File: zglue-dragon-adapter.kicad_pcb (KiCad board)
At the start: 6 copper layers, 25 x 20 mm, 56 parts, among them J1 543630489, J2 543630489, U1 zGlue-Dragon

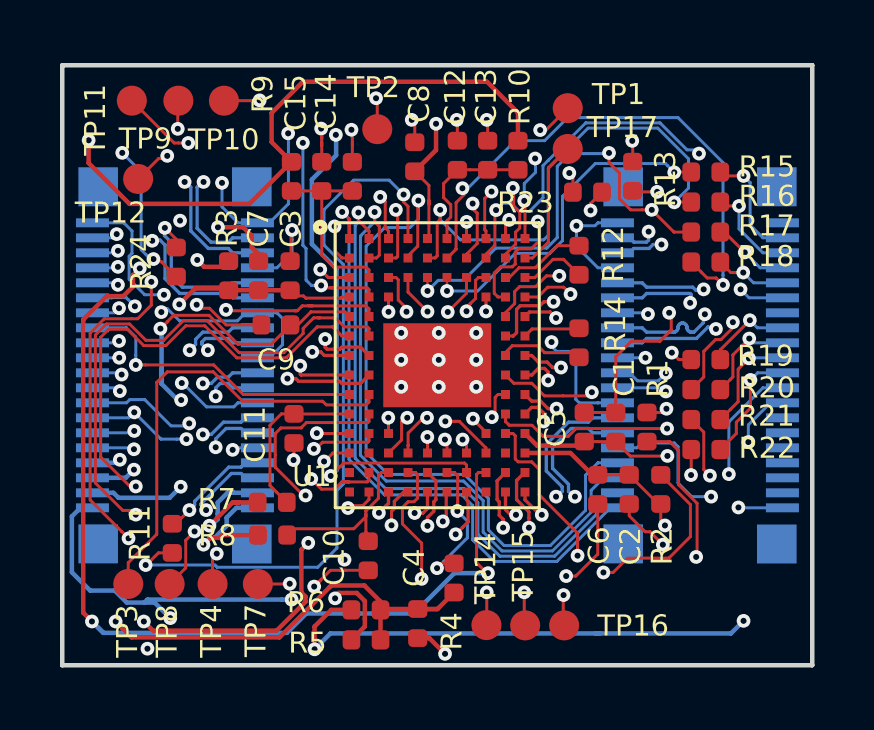
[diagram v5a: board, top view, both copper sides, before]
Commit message: Layout polishing, connected PROC_RST and CTRL_RST to chip via 0R
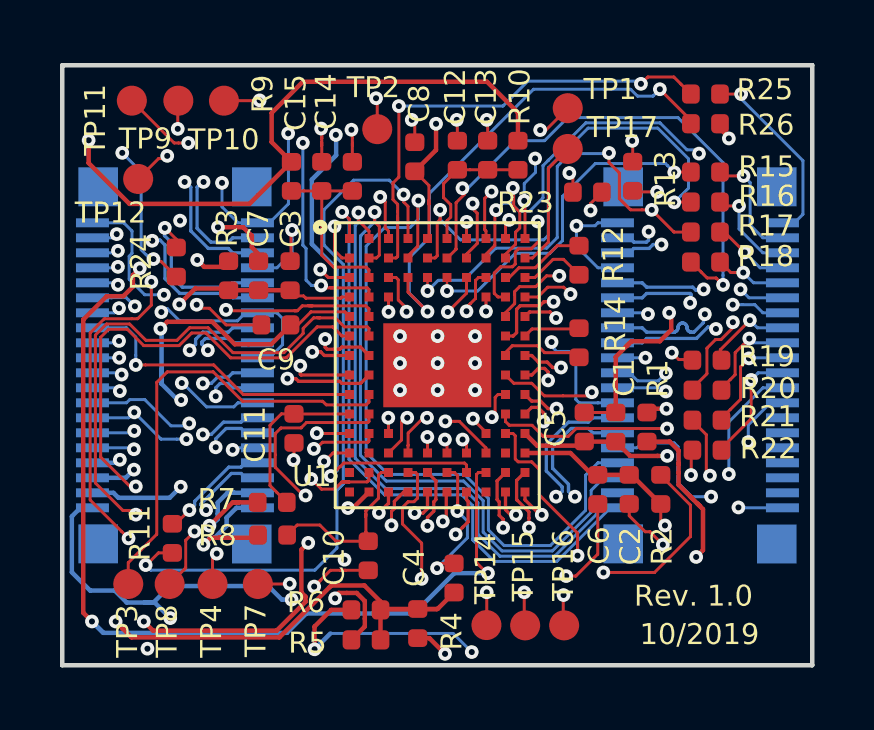
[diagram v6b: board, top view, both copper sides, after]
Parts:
- added R25: R_0R_0402, antmicro-footprints:0402-res, F.Cu at (21.4, 0.96)
- added R26: R_0R_0402, antmicro-footprints:0402-res, F.Cu at (21.4, 1.95)
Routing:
- net /CTRL_RST: track 1.40 -> 16.8 mm, vias 1 -> 2
- net /PROC_RST: track 2.05 -> 16.1 mm, vias 1 -> 2
- net /CTRL_RST_FLASH_SOC_CS: track 0.00 -> 9.34 mm, vias 0 -> 2
- net /E_PROC_RST: track 0.00 -> 6.37 mm, vias 0 -> 1
- net /3V3: track 39.6 -> 41.0 mm
- net /1V2_SYS_B: track 49.8 -> 48.8 mm
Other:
- board text added: "10/2019"
- board text added: "Rev. 1.0"

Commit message: Added testpad for VSENSE
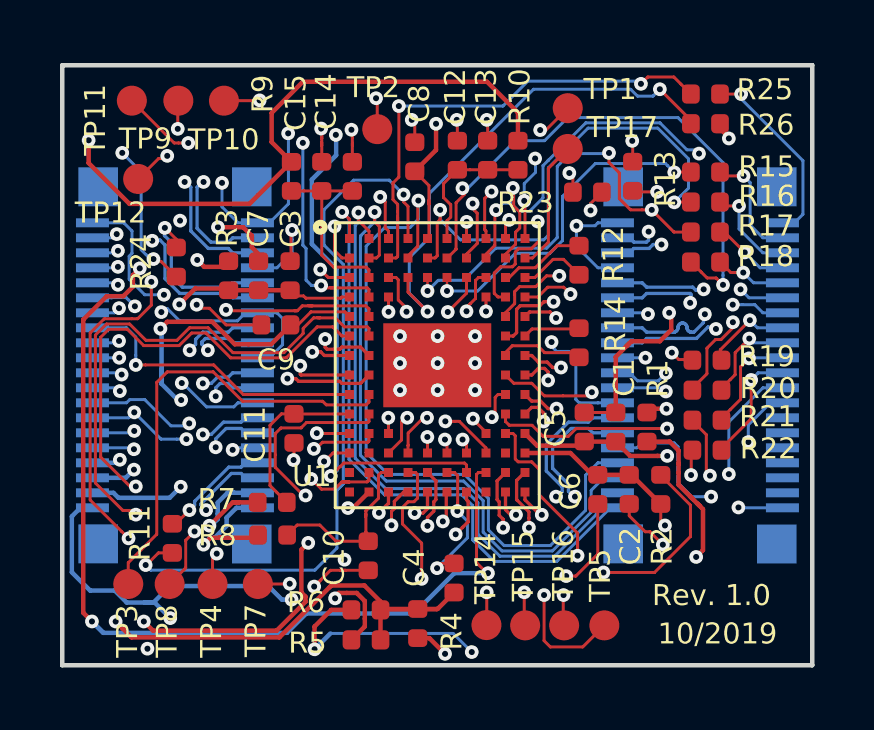
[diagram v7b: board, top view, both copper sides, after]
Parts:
- added TP5: TP_SMD1MM, antmicro-footprints:Testpoint_smd_1mm, F.Cu at (18.1, 18.7)
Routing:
- net /VSENSE: track 1.30 -> 16.1 mm, vias 1 -> 2

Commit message: Moved C1,2,3,4 closer to LDO output pins
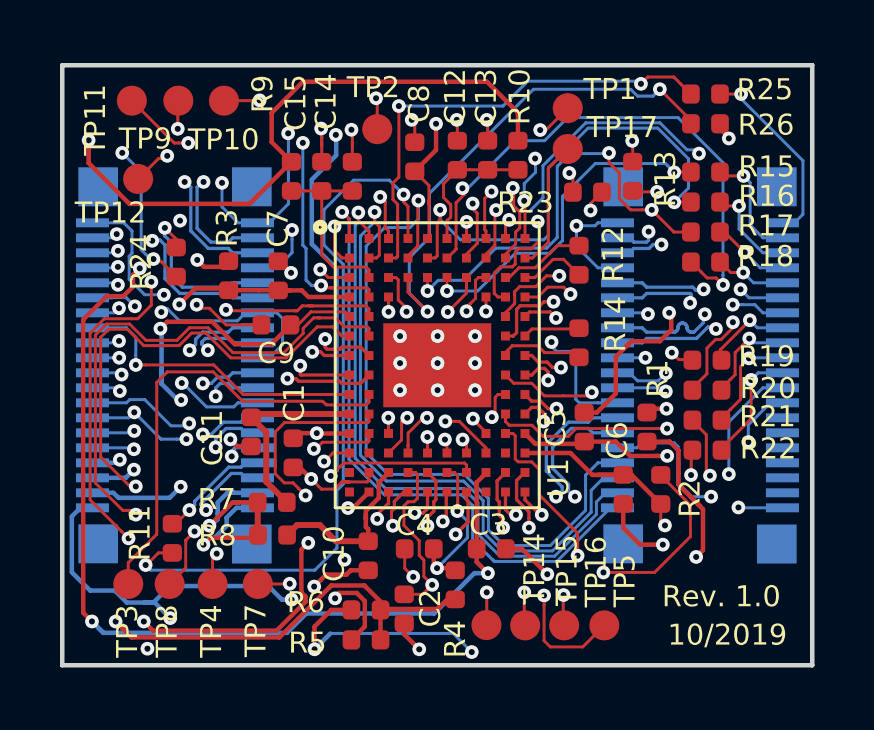
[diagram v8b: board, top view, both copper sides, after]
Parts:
- moved C3 11.3 mm to (14.3, 16.1), turned to 0 degrees
- moved C1 10.8 mm to (7.70, 12.9), turned to 270 degrees
- moved C2 8.49 mm to (11.4, 18.1)
- moved C4 2.49 mm to (11.9, 16.1), turned to 180 degrees
- moved C11 1.43 mm to (6.30, 12.2)
- moved C6 0.85 mm to (18.7, 14.1)
- moved C7 0.66 mm to (7.20, 7.02)
- moved R4 0.23 mm to (13.1, 17.3)
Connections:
- C1 pad 1: /3V3_SYS -> /3V3
- C2 pad 1: /1V8_SYS -> /1V8
- C3 pad 1: /2V5_SYS -> /2V5
- C4 pad 1: /1V2_SYS -> /1V2
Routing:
- net /VBATH: track 5.61 -> 9.09 mm
- net /2V5: track 34.9 -> 37.8 mm
- net GND: track 72.5 -> 70.1 mm, vias 42 -> 43
- net /1V8: track 16.7 -> 18.5 mm
- net /VSENSE: track 16.1 -> 17.7 mm
- net /VUSB: track 9.50 -> 10.6 mm
- net /1V8_SYS: track 32.4 -> 33.4 mm
- net /3V3: track 41.0 -> 41.9 mm
- net /2V5_SYS: track 15.9 -> 16.7 mm
- net /1V2: track 4.68 -> 5.38 mm
